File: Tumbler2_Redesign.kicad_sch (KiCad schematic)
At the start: 4 parts

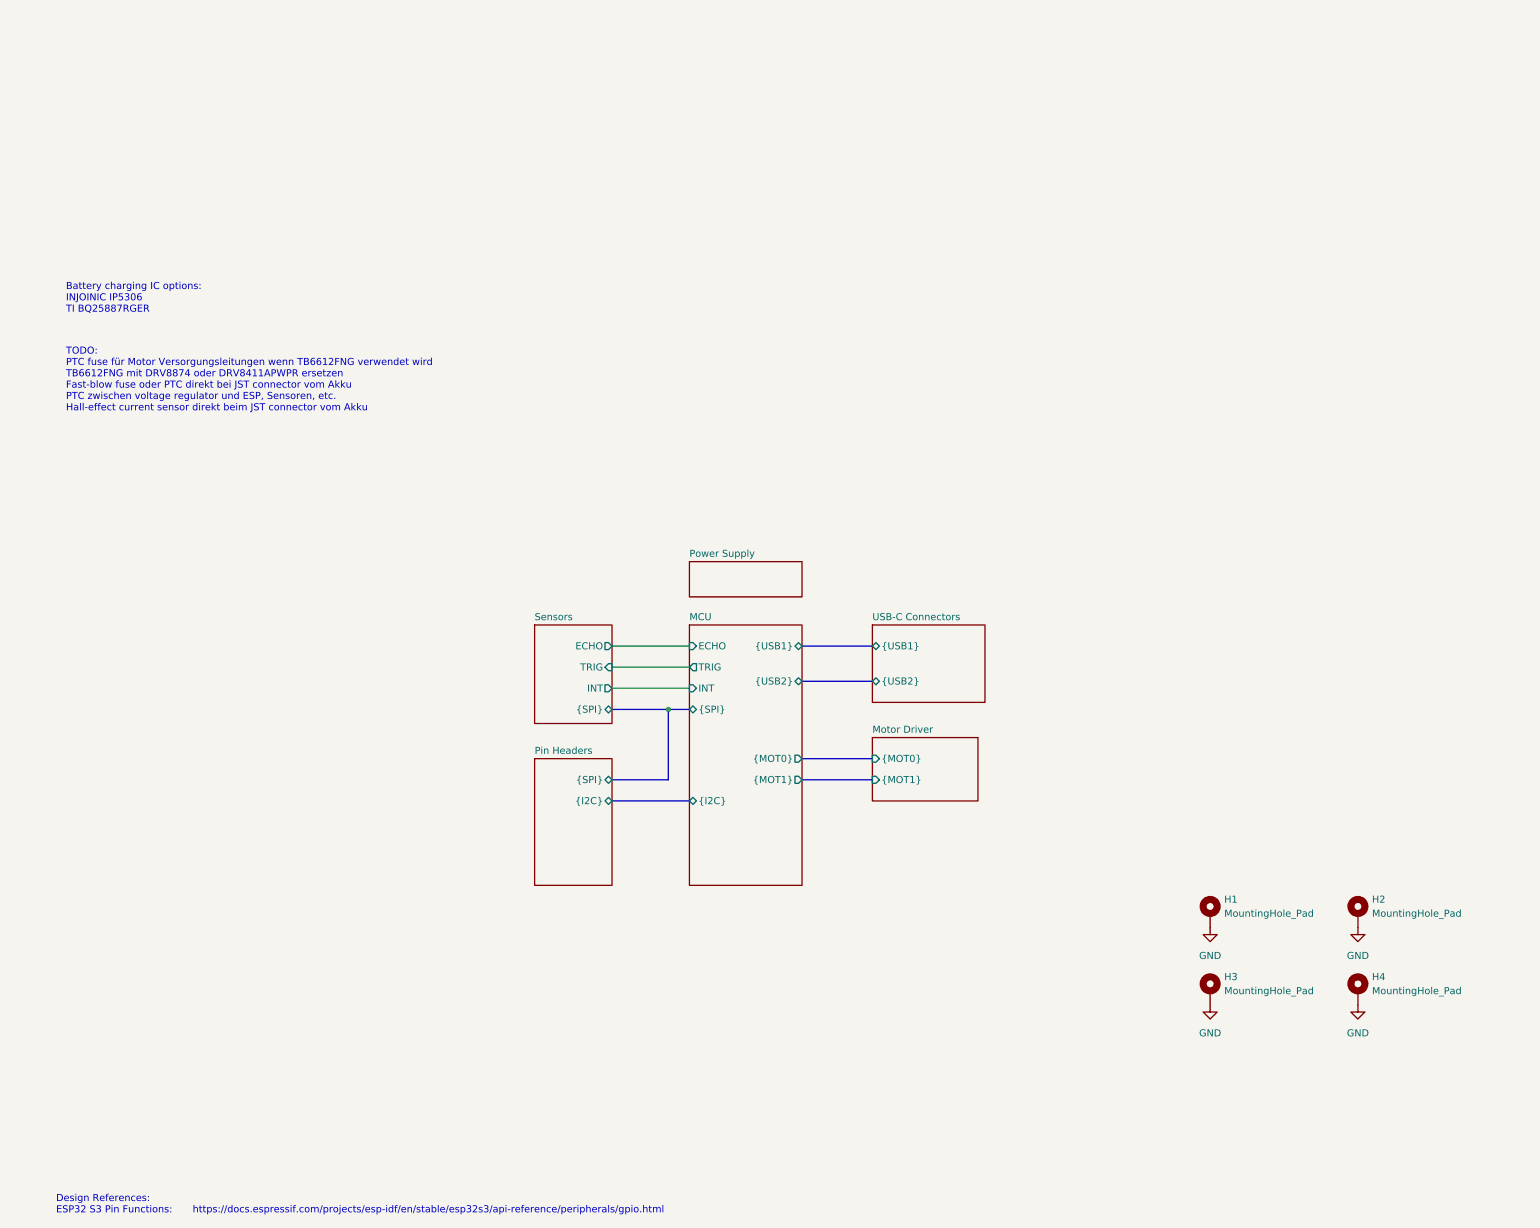
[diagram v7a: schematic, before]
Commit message: Update TODO entries
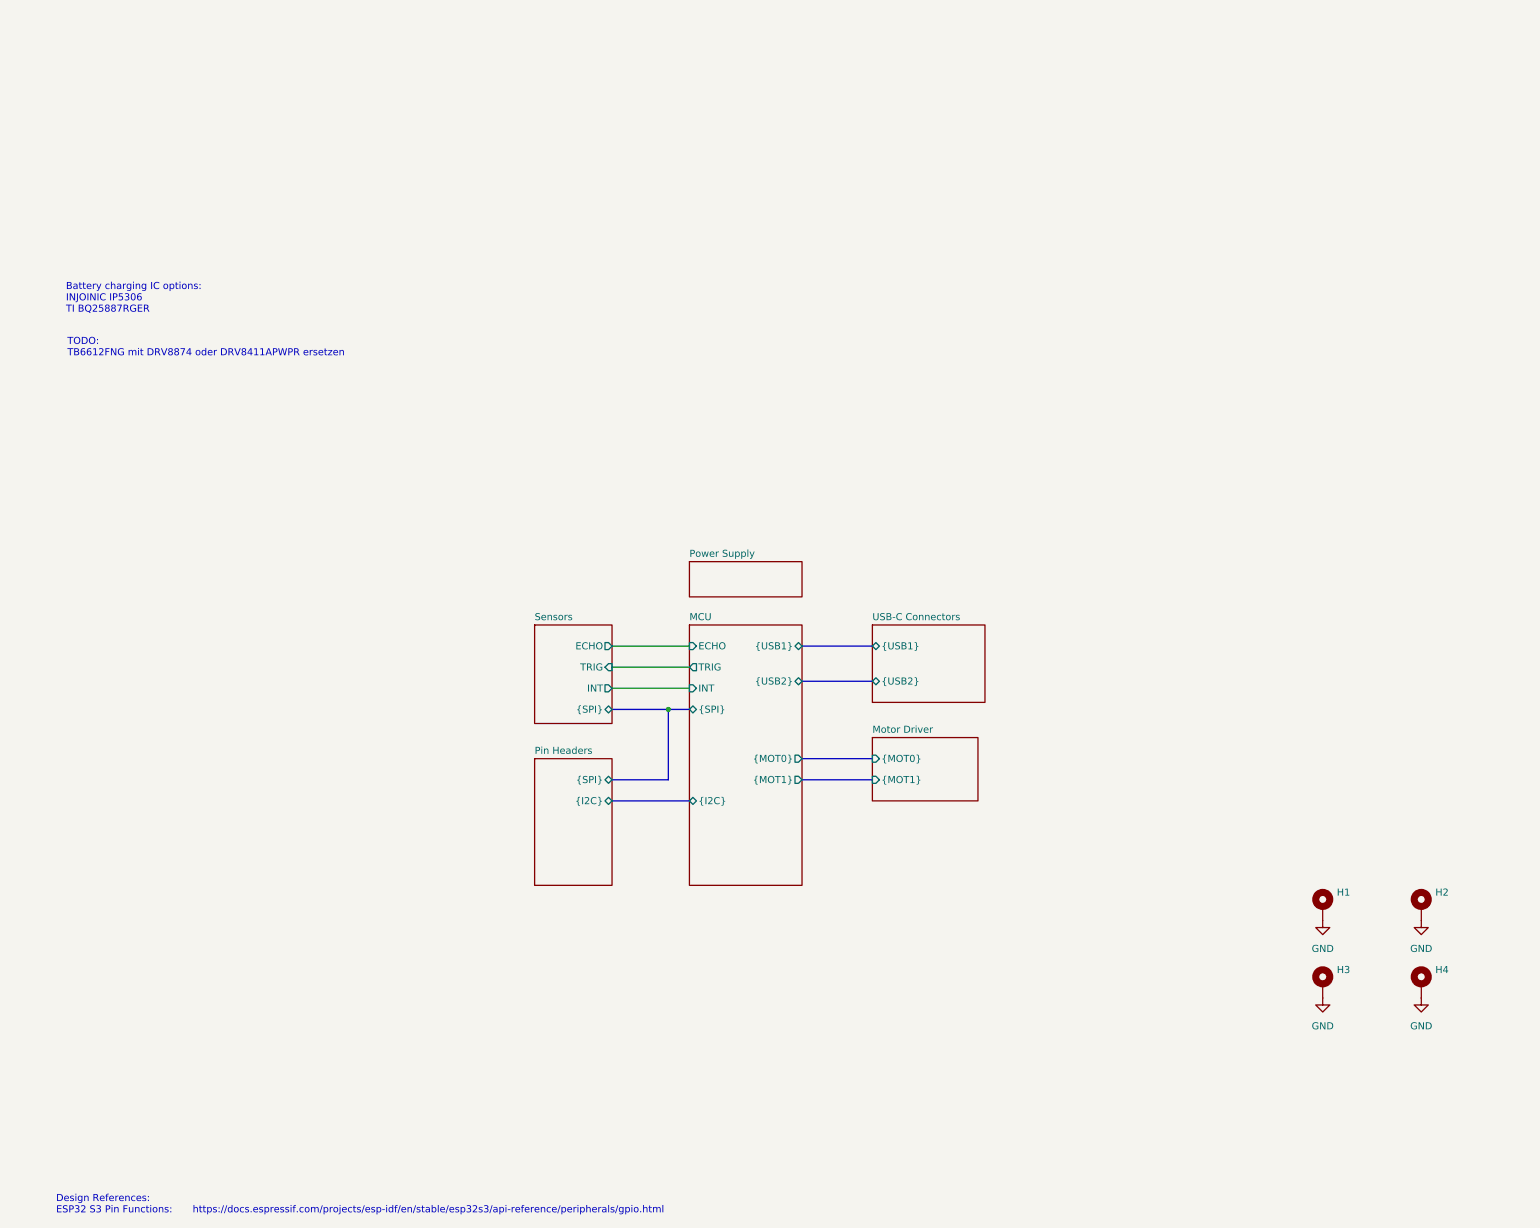
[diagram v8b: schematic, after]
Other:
- note added: "TODO: TB6612FNG mit DRV8874 oder DRV8411APWPR ersetzen"
- note removed: "TODO: PTC fuse für Motor Versorgungsleitungen wenn TB6612FNG verwendet wird TB6612FNG mit DRV8874 oder DRV8411APWPR ersetzen Fast-blow fuse oder PTC direkt bei JST connector vom Akku PTC zwischen voltage regulator und ESP, Sensoren, etc. Hall-effect current sensor direkt beim JST connector vom Akku"
- moved on the sheet: H1, H2, H3, H4
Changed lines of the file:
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@@
 		)
 	)
-	(text "TODO:\nPTC fuse für Motor Versorgungsleitungen wenn TB6612FNG verwendet wird\nTB6612FNG mit DRV8874 oder DRV8411APWPR ersetzen\nFast-blow fuse oder PTC direkt bei JST connector vom Akku\nPTC zwischen voltage regulator und ESP, Sensoren, etc.\nHall-effect current sensor direkt beim JST connector vom Akku\n"
-		(exclude_from_sim no)
-		(at 20.828 39.624 0)
+	(text "TODO:\nTB6612FNG mit DRV8874 oder DRV8411APWPR ersetzen\n"
+		(exclude_from_sim no)
+		(at 21.082 33.782 0)
 		(effects
 			(font
@@
 	(symbol
 		(lib_id "Mechanical:MountingHole_Pad")
-		(at 227.33 149.86 0)
+		(at 247.65 148.59 0)
 		(unit 1)
 		(exclude_from_sim no)
@@
 		(fields_autoplaced yes)
 		(property "Reference" "H3"
-			(at 229.87 147.3199 0)
+			(at 250.19 146.0499 0)
 			(effects
 				(font
@@
 		)
 		(property "Value" "MountingHole_Pad"
-			(at 229.87 149.8599 0)
-			(effects
-				(font
-					(size 1.27 1.27)
-				)
-				(justify left)
+			(at 250.19 148.5899 0)
+			(effects
+				(font
+					(size 1.27 1.27)
+				)
+				(justify left)
+				(hide yes)
 			)
 		)
 		(property "Footprint" "MountingHole:MountingHole_3mm_Pad"
-			(at 227.33 149.86 0)
+			(at 247.65 148.59 0)
 			(effects
 				(font
@@
 		)
 		(property "Datasheet" "~"
-			(at 227.33 149.86 0)
+			(at 247.65 148.59 0)
 			(effects
 				(font
@@
 		)
 		(property "Description" "Mounting Hole with connection"
-			(at 227.33 149.86 0)
+			(at 247.65 148.59 0)
 			(effects
 				(font
@@
 	(symbol
 		(lib_id "power:GND")
-		(at 254 152.4 0)
+		(at 265.43 151.13 0)
 		(unit 1)
 		(exclude_from_sim no)
@@
 		(fields_autoplaced yes)
 		(property "Reference" "#PWR029"
-			(at 254 158.75 0)
+			(at 265.43 157.48 0)
 			(effects
 				(font
@@
 		)
 		(property "Value" "GND"
-			(at 254 157.48 0)
+			(at 265.43 156.21 0)
 			(effects
 				(font
@@
 		)
 		(property "Footprint" ""
-			(at 254 152.4 0)
+			(at 265.43 151.13 0)
 			(effects
 				(font
@@
 		)
 		(property "Datasheet" ""
-			(at 254 152.4 0)
+			(at 265.43 151.13 0)
 			(effects
 				(font
@@
 		)
 		(property "Description" "Power symbol creates a global label with name \"GND\" , ground"
-			(at 254 152.4 0)
+			(at 265.43 151.13 0)
 			(effects
 				(font
@@
 	(symbol
 		(lib_id "Mechanical:MountingHole_Pad")
-		(at 254 149.86 0)
+		(at 265.43 148.59 0)
 		(unit 1)
 		(exclude_from_sim no)
@@
 		(fields_autoplaced yes)
 		(property "Reference" "H4"
-			(at 256.54 147.3199 0)
+			(at 267.97 146.0499 0)
 			(effects
 				(font
@@
 		)
 		(property "Value" "MountingHole_Pad"
-			(at 256.54 149.8599 0)
-			(effects
-				(font
-					(size 1.27 1.27)
-				)
-				(justify left)
+			(at 267.97 148.5899 0)
+			(effects
+				(font
+					(size 1.27 1.27)
+				)
+				(justify left)
+				(hide yes)
 			)
 		)
 		(property "Footprint" "MountingHole:MountingHole_3mm_Pad"
-			(at 254 149.86 0)
+			(at 265.43 148.59 0)
 			(effects
 				(font
@@
 		)
 		(property "Datasheet" "~"
-			(at 254 149.86 0)
+			(at 265.43 148.59 0)
 			(effects
 				(font
@@
 		)
 		(property "Description" "Mounting Hole with connection"
-			(at 254 149.86 0)
+			(at 265.43 148.59 0)
 			(effects
 				(font
@@
 	(symbol
 		(lib_id "Mechanical:MountingHole_Pad")
-		(at 254 135.89 0)
+		(at 265.43 134.62 0)
 		(unit 1)
 		(exclude_from_sim no)
@@
 		(fields_autoplaced yes)
 		(property "Reference" "H2"
-			(at 256.54 133.3499 0)
+			(at 267.97 132.0799 0)
 			(effects
 				(font
@@
 		)
 		(property "Value" "MountingHole_Pad"
-			(at 256.54 135.8899 0)
-			(effects
-				(font
-					(size 1.27 1.27)
-				)
-				(justify left)
+			(at 267.97 134.6199 0)
+			(effects
+				(font
+					(size 1.27 1.27)
+				)
+				(justify left)
+				(hide yes)
 			)
 		)
 		(property "Footprint" "MountingHole:MountingHole_3mm_Pad"
-			(at 254 135.89 0)
+			(at 265.43 134.62 0)
 			(effects
 				(font
@@
 		)
 		(property "Datasheet" "~"
-			(at 254 135.89 0)
+			(at 265.43 134.62 0)
 			(effects
 				(font
@@
 		)
 		(property "Description" "Mounting Hole with connection"
-			(at 254 135.89 0)
+			(at 265.43 134.62 0)
 			(effects
 				(font
@@
 	(symbol
 		(lib_id "power:GND")
-		(at 227.33 152.4 0)
+		(at 247.65 151.13 0)
 		(unit 1)
 		(exclude_from_sim no)
@@
 		(fields_autoplaced yes)
 		(property "Reference" "#PWR028"
-			(at 227.33 158.75 0)
+			(at 247.65 157.48 0)
 			(effects
 				(font
@@
 		)
 		(property "Value" "GND"
-			(at 227.33 157.48 0)
+			(at 247.65 156.21 0)
 			(effects
 				(font
@@
 		)
 		(property "Footprint" ""
-			(at 227.33 152.4 0)
+			(at 247.65 151.13 0)
 			(effects
 				(font
@@
 		)
 		(property "Datasheet" ""
-			(at 227.33 152.4 0)
+			(at 247.65 151.13 0)
 			(effects
 				(font
@@
 		)
 		(property "Description" "Power symbol creates a global label with name \"GND\" , ground"
-			(at 227.33 152.4 0)
+			(at 247.65 151.13 0)
 			(effects
 				(font
@@
 	(symbol
 		(lib_id "Mechanical:MountingHole_Pad")
-		(at 227.33 135.89 0)
+		(at 247.65 134.62 0)
 		(unit 1)
 		(exclude_from_sim no)
@@
 		(fields_autoplaced yes)
 		(property "Reference" "H1"
-			(at 229.87 133.3499 0)
+			(at 250.19 132.0799 0)
 			(effects
 				(font
@@
 		)
 		(property "Value" "MountingHole_Pad"
-			(at 229.87 135.8899 0)
-			(effects
-				(font
-					(size 1.27 1.27)
-				)
-				(justify left)
+			(at 250.19 134.6199 0)
+			(effects
+				(font
+					(size 1.27 1.27)
+				)
+				(justify left)
+				(hide yes)
 			)
 		)
 		(property "Footprint" "MountingHole:MountingHole_3mm_Pad"
-			(at 227.33 135.89 0)
+			(at 247.65 134.62 0)
 			(effects
 				(font
@@
 		)
 		(property "Datasheet" "~"
-			(at 227.33 135.89 0)
+			(at 247.65 134.62 0)
 			(effects
 				(font
@@
 		)
 		(property "Description" "Mounting Hole with connection"
-			(at 227.33 135.89 0)
+			(at 247.65 134.62 0)
 			(effects
 				(font
@@
 	(symbol
 		(lib_id "power:GND")
-		(at 254 138.43 0)
+		(at 265.43 137.16 0)
 		(unit 1)
 		(exclude_from_sim no)
@@
 		(fields_autoplaced yes)
 		(property "Reference" "#PWR027"
-			(at 254 144.78 0)
+			(at 265.43 143.51 0)
 			(effects
 				(font
@@
 		)
 		(property "Value" "GND"
-			(at 254 143.51 0)
+			(at 265.43 142.24 0)
 			(effects
 				(font
@@
 		)
 		(property "Footprint" ""
-			(at 254 138.43 0)
+			(at 265.43 137.16 0)
 			(effects
 				(font
@@
 		)
 		(property "Datasheet" ""
-			(at 254 138.43 0)
+			(at 265.43 137.16 0)
 			(effects
 				(font
@@
 		)
 		(property "Description" "Power symbol creates a global label with name \"GND\" , ground"
-			(at 254 138.43 0)
+			(at 265.43 137.16 0)
 			(effects
 				(font
@@
 	(symbol
 		(lib_id "power:GND")
-		(at 227.33 138.43 0)
+		(at 247.65 137.16 0)
 		(unit 1)
 		(exclude_from_sim no)
@@
 		(fields_autoplaced yes)
 		(property "Reference" "#PWR026"
-			(at 227.33 144.78 0)
+			(at 247.65 143.51 0)
 			(effects
 				(font
@@
 		)
 		(property "Value" "GND"
-			(at 227.33 143.51 0)
+			(at 247.65 142.24 0)
 			(effects
 				(font
@@
 		)
 		(property "Footprint" ""
-			(at 227.33 138.43 0)
+			(at 247.65 137.16 0)
 			(effects
 				(font
@@
 		)
 		(property "Datasheet" ""
-			(at 227.33 138.43 0)
+			(at 247.65 137.16 0)
 			(effects
 				(font
@@
 		)
 		(property "Description" "Power symbol creates a global label with name \"GND\" , ground"
-			(at 227.33 138.43 0)
-			(effects
-				(font
+			(at 247.65 137.16 0)
+			(effects
+				(font
